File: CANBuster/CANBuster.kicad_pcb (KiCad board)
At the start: 2 copper layers, 100 x 100 mm, 182 parts, among them CON1 BARREL_JACK, J1 RJ45, J2 RJ45, J3 RJ12, P1 CONN_01X10, P10 CONN_02X04, P11 RS232-Programmer, P12 S88, P13 CONN_01X10, P14 CONN_01X10, P15 TRACK, P16 CONN_01X02, P17 USB_OTG, P18 CONN_01X04, P2 CONN_01X10, P3 CONN_01X03, P4 CONN_01X03, P5 CONN_01X03, P6 CONN_01X03, P7 CONN_01X02, P8 CONN_01X06, P9 CONN_01X04, Q1 BC547, Q2 BC547, SW1 SW_PUSH, SW2 SW_PUSH, U1 PIC18F45K80, U12 MCP2561, U2 MCP2561, U3 7805, U4 LTV-844, U5 LTV-844, U6 LTV-844, U7 LTV-844, U8 ISO1050, Y1 16MHz

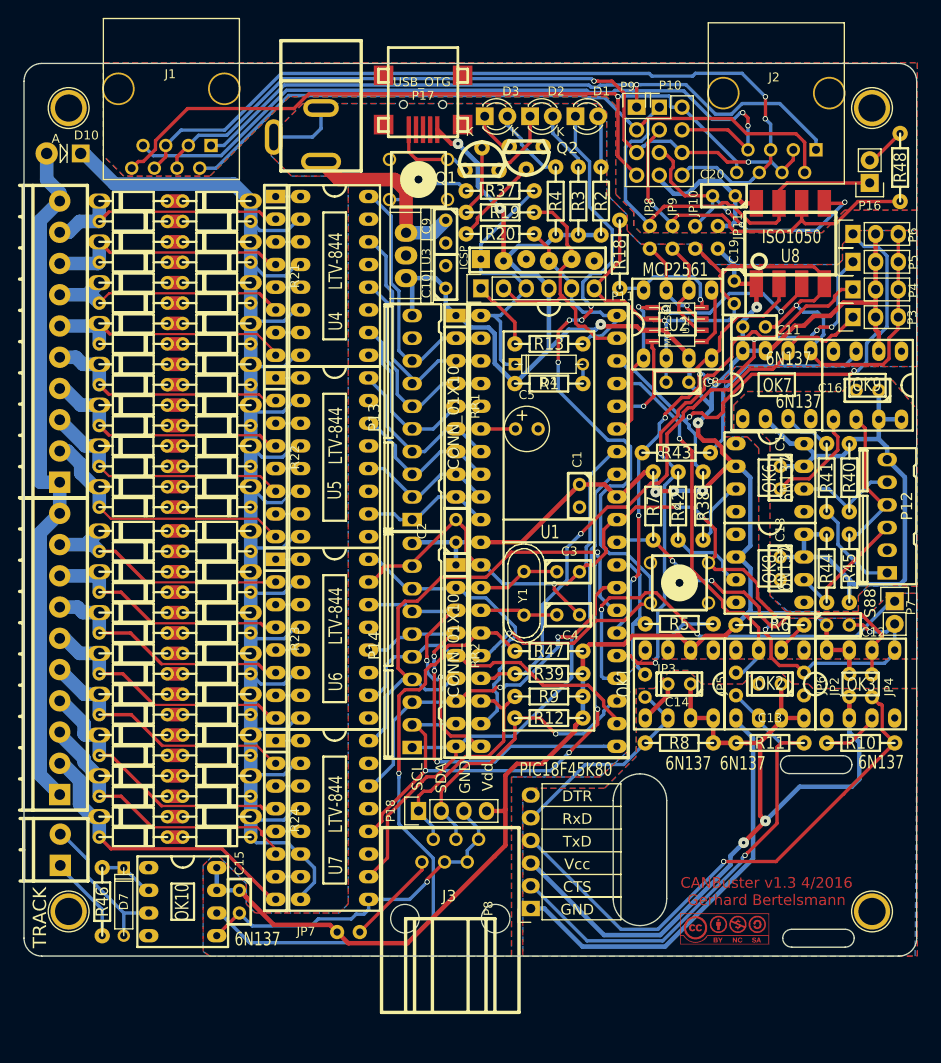
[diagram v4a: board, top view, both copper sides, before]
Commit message: fixed I2C connector
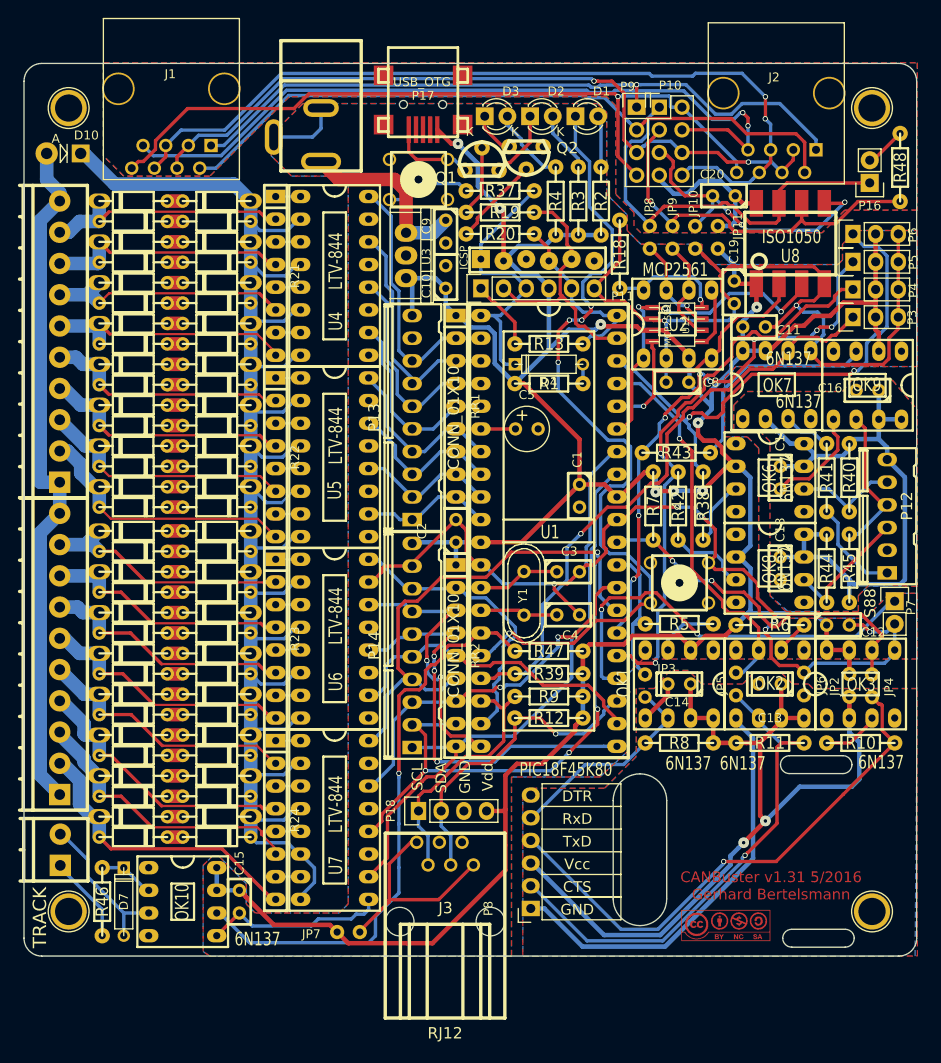
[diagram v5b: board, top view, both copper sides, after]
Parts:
- J3: footprint w_conn_misc:6p6c -> w_conn_misc:molex_6p6c
- moved J3 0.67 mm to (117.3, 131.3)
- moved G*** 0.40 mm to (148.7, 131.7)
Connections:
- J3 pad 6: GND -> Net-(J3-Pad1)
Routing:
- net GND: track 258.1 -> 238.6 mm, vias 9 -> 8
- net VDD: track 337.7 -> 354.2 mm
- net Net-(J3-Pad1): track 10.7 -> 24.1 mm
- net /SNIFF: track 71.2 -> 65.4 mm
- net /SCL: track 26.0 -> 28.8 mm
- net /SDA: track 33.0 -> 35.7 mm
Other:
- board text added: "CANBuster v1.31 5/2016 Gerhard Bertelsmann"
- board text removed: "CANBuster v1.3 4/2016 Gerhard Bertelsmann"

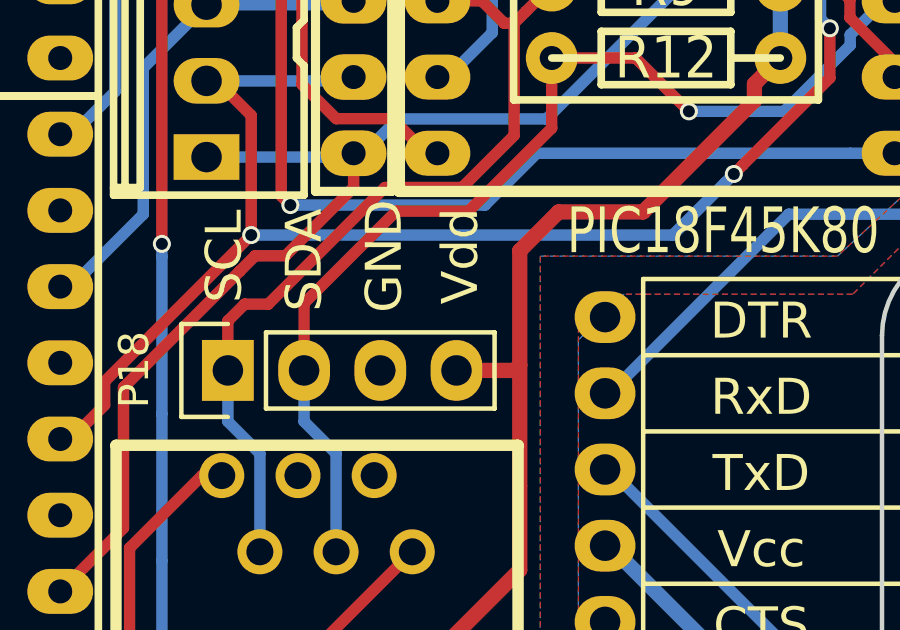
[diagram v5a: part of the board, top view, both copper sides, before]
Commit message: change I2C pin header for easy connect of cheap I2C display
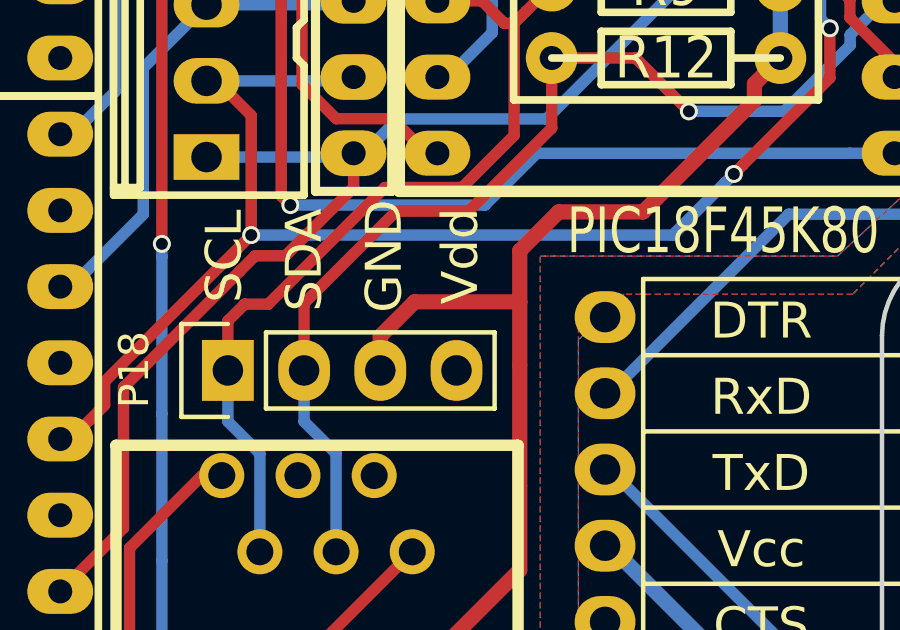
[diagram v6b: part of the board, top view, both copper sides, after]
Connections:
- P18 pad 3: GND -> VDD
- P18 pad 4: VDD -> GND
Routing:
- net VDD: track 354.2 -> 358.3 mm

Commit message: update parts
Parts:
- R10: value 220 -> 270
- R11, R8: value 390 -> 1k
- R43: value 330 -> 390
- moved C5 1.52 mm to (125.4, 74.6)
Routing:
- net VDD: track 358.3 -> 359.7 mm
- net Net-(C5-Pad1): track 3.87 -> 4.76 mm
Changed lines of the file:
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@@
-(kicad_pcb (version 4) (host pcbnew "(2015-06-12 BZR 5742)-product")
+(kicad_pcb (version 4) (host pcbnew 4.0.2+dfsg1-stable)
   (general
     (links 464)
@@
     (thickness 1.6)
     (drawings 39)
-    (tracks 1782)
+    (tracks 1785)
     (zones 0)
     (modules 182)
@@
   )
   (module Capacitors_Elko_ThroughHole:Elko_vert_11x5mm_RM2.5 (layer F.Cu)
-    (at 125.1585 76.073)
+    (at 125.4252 74.5744)
     (descr "Electrolytic Capacitor, vertical, diameter 5mm, radial, RM 2,5mm")
     (tags "Electrolytic Capacitor, vertical, diameter 5mm, radial, RM 2,5mm, Elko, Electrolytkondensator, Kondensator gepolt, Durchmesser 5mm")
@@
   (module Wire_Pads:SolderWirePad_2x_0-2.54mmDrill (layer F.Cu)
     (at 139.6746 104.8512 270)
-    (fp_text reference JP3 (at -1.905 -2.413 360) (layer F.SilkS)
+    (fp_text reference JP3 (at -2.2098 -2.5146 360) (layer F.SilkS)
       (effects (font (size 1 1) (thickness 0.15)))
     )
@@
       (effects (font (size 1.397 1.27) (thickness 0.2032)))
     )
-    (fp_text value 390 (at 0 2.032) (layer F.SilkS) hide
+    (fp_text value 1k (at 0 2.032) (layer F.SilkS) hide
       (effects (font (size 1.397 1.27) (thickness 0.2032)))
     )
@@
       (effects (font (size 1.397 1.27) (thickness 0.2032)))
     )
-    (fp_text value 220 (at 0 2.032 180) (layer F.SilkS) hide
+    (fp_text value 270 (at 0 2.032 180) (layer F.SilkS) hide
       (effects (font (size 1.397 1.27) (thickness 0.2032)))
     )
@@
       (effects (font (size 1.397 1.27) (thickness 0.2032)))
     )
-    (fp_text value 390 (at 0 2.032) (layer F.SilkS) hide
+    (fp_text value 1k (at 0 2.032) (layer F.SilkS) hide
       (effects (font (size 1.397 1.27) (thickness 0.2032)))
     )
@@
       (effects (font (size 1.397 1.27) (thickness 0.2032)))
     )
-    (fp_text value 330 (at 0 2.032 180) (layer F.SilkS) hide
+    (fp_text value 390 (at 0 2.032 180) (layer F.SilkS) hide
       (effects (font (size 1.397 1.27) (thickness 0.2032)))
     )
@@
     (descr "IC, DIL8 x 0,3\", with socket")
     (tags DIL)
-    (fp_text reference OK2 (at 0.0635 0.0635 180) (layer F.SilkS)
+    (fp_text reference OK2 (at 3.4544 -8.636 180) (layer F.SilkS)
       (effects (font (size 1.524 1.143) (thickness 0.28702)))
     )
-    (fp_text value 6N137 (at 3.048 -8.89 180) (layer F.SilkS)
+    (fp_text value 6N137 (at 3.1496 -10.4648 180) (layer F.SilkS)
       (effects (font (size 1.524 1.143) (thickness 0.28702)))
     )
@@
     (descr "Small ceramic capacitor")
     (tags C)
-    (fp_text reference C13 (at 0 -3.81 180) (layer F.SilkS)
+    (fp_text reference C13 (at 0.508 2.0828 180) (layer F.SilkS)
       (effects (font (size 1.016 1.016) (thickness 0.2032)))
     )
@@
     (descr "Small ceramic capacitor")
     (tags C)
-    (fp_text reference C14 (at 0.254 -2.032 180) (layer F.SilkS)
+    (fp_text reference C14 (at -2.0066 1.9812 180) (layer F.SilkS)
       (effects (font (size 1.016 1.016) (thickness 0.2032)))
     )
@@
     (descr "Small ceramic capacitor")
     (tags C)
-    (fp_text reference C2 (at 0 -3.81 90) (layer F.SilkS)
+    (fp_text reference C2 (at 1.1684 -2.6924 90) (layer F.SilkS)
       (effects (font (size 1.016 1.016) (thickness 0.2032)))
     )
@@
   (gr_arc (start 168.104 133.128) (end 170.104 133.128) (angle 90) (layer Edge.Cuts) (width 0.15))
   (gr_arc (start 72.104 133.128) (end 72.104 135.128) (angle 90) (layer Edge.Cuts) (width 0.15))
+  (segment (start 126.0856 70.993) (end 128.4986 70.993) (width 0.508) (layer F.Cu) (net 1))
+  (segment (start 125.095 70.993) (end 126.0856 70.993) (width 0.508) (layer F.Cu) (net 1))
+  (segment (start 132.334 77.2414) (end 132.334 82.296) (width 0.508) (layer F.Cu) (net 1))
+  (segment (start 132.334 74.8284) (end 132.334 77.2414) (width 0.508) (layer F.Cu) (net 1))
+  (segment (start 128.4986 70.993) (end 132.334 74.8284) (width 0.508) (layer F.Cu) (net 1))
   (segment (start 119.38 118.872) (end 119.38 117.729) (width 0.508) (layer F.Cu) (net 1))
   (segment (start 120.523 116.586) (end 124.0282 116.586) (width 0.508) (layer F.Cu) (net 1))
@@
   (segment (start 124.0282 122.725018) (end 124.0282 125.5268) (width 0.508) (layer F.Cu) (net 1))
   (segment (start 106.435401 133.689601) (end 113.063617 133.689601) (width 0.508) (layer F.Cu) (net 1))
-  (segment (start 126.0856 70.993) (end 132.334 77.2414) (width 0.508) (layer F.Cu) (net 1))
-  (segment (start 132.334 77.2414) (end 132.334 82.296) (width 0.508) (layer F.Cu) (net 1))
-  (segment (start 125.095 70.993) (end 126.0856 70.993) (width 0.508) (layer F.Cu) (net 1))
   (segment (start 168.0464 60.452) (end 168.0464 57.3532) (width 0.381) (layer F.Cu) (net 2))
   (segment (start 168.0464 63.5508) (end 168.0464 60.452) (width 0.381) (layer F.Cu) (net 2))
@@
   (segment (start 121.285 96.393) (end 125.57506 96.393) (width 0.381) (layer F.Cu) (net 4))
   (segment (start 125.57506 96.393) (end 126.111 96.92894) (width 0.381) (layer F.Cu) (net 4))
-  (segment (start 121.285 76.073) (end 125.1585 76.073) (width 0.381) (layer F.Cu) (net 5))
+  (segment (start 121.285 76.073) (end 123.9266 76.073) (width 0.381) (layer F.Cu) (net 5))
+  (segment (start 123.9266 76.073) (end 125.4252 74.5744) (width 0.381) (layer F.Cu) (net 5))
   (segment (start 121.285 55.372) (end 121.285 55.6514) (width 0.381) (layer B.Cu) (net 6))
   (segment (start 121.285 55.6514) (end 121.285 57.0484) (width 0.381) (layer B.Cu) (net 6))

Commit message: store
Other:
- board text added: "CANBuster v1.31 12/2016 Gerhard Bertelsmann"
- board text removed: "CANBuster v1.31 5/2016 Gerhard Bertelsmann"
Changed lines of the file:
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@@
     (links 464)
     (no_connects 0)
-    (area 70.028999 35.052999 170.179001 135.203001)
+    (area 69.215499 29.4545 181.99 145.18574)
     (thickness 1.6)
     (drawings 39)
-    (tracks 1785)
+    (tracks 1784)
     (zones 0)
     (modules 182)
@@
     (effects (font (size 1.2 1.2) (thickness 0.2)))
   )
-  (gr_text "CANBuster v1.31 5/2016\nGerhard Bertelsmann" (at 153.797 127.254) (layer F.Cu)
+  (gr_text "CANBuster v1.31 12/2016\nGerhard Bertelsmann" (at 154.304 126.678) (layer F.Cu)
     (effects (font (size 1.2 1.2) (thickness 0.25)))
   )
@@
   (segment (start 161.274101 76.966421) (end 160.782 76.47432) (width 0.381) (layer F.Cu) (net 47))
   (segment (start 160.782 76.47432) (end 160.782 74.9935) (width 0.381) (layer F.Cu) (net 47))
+  (segment (start 126.873 119.634) (end 131.318 119.634) (width 0.381) (layer B.Cu) (net 48))
+  (segment (start 137.287 113.665) (end 139.7 111.252) (width 0.381) (layer B.Cu) (net 48))
+  (segment (start 131.318 119.634) (end 137.287 113.665) (width 0.381) (layer B.Cu) (net 48))
   (segment (start 139.6746 106.1212) (end 139.9032 106.1212) (width 0.381) (layer B.Cu) (net 48))
   (segment (start 139.9032 106.1212) (end 142.24 108.458) (width 0.381) (layer B.Cu) (net 48))
@@
   (segment (start 139.7 111.252) (end 142.24 108.712) (width 0.381) (layer B.Cu) (net 48))
   (segment (start 142.24 108.712) (end 142.24 108.458) (width 0.381) (layer B.Cu) (net 48))
-  (segment (start 132.9944 113.665) (end 137.287 113.665) (width 0.381) (layer B.Cu) (net 48))
-  (segment (start 137.287 113.665) (end 139.7 111.252) (width 0.381) (layer B.Cu) (net 48))
-  (segment (start 126.873 119.634) (end 127.0254 119.634) (width 0.381) (layer B.Cu) (net 48))
-  (segment (start 127.0254 119.634) (end 132.9944 113.665) (width 0.381) (layer B.Cu) (net 48))
   (segment (start 164.719 93.472) (end 163.068 93.472) (width 0.508) (layer B.Cu) (net 49))
   (segment (start 163.068 93.472) (end 162.56 92.964) (width 0.508) (layer B.Cu) (net 49))
